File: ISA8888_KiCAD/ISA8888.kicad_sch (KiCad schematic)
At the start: 65 parts, among them J1 Bus_PCI_32bit_Universal, J2 Bus_ISA_16bit, J3 AEN/BALE/TC J3, J4 Crystal J4, J5 PCI Jumpers, J6 PPDGNT# Motherboard Redirect, J7 PPDREQ# Motherboard Redirect, U2 SMROM-AT24CS02, Y1 CFPS-72

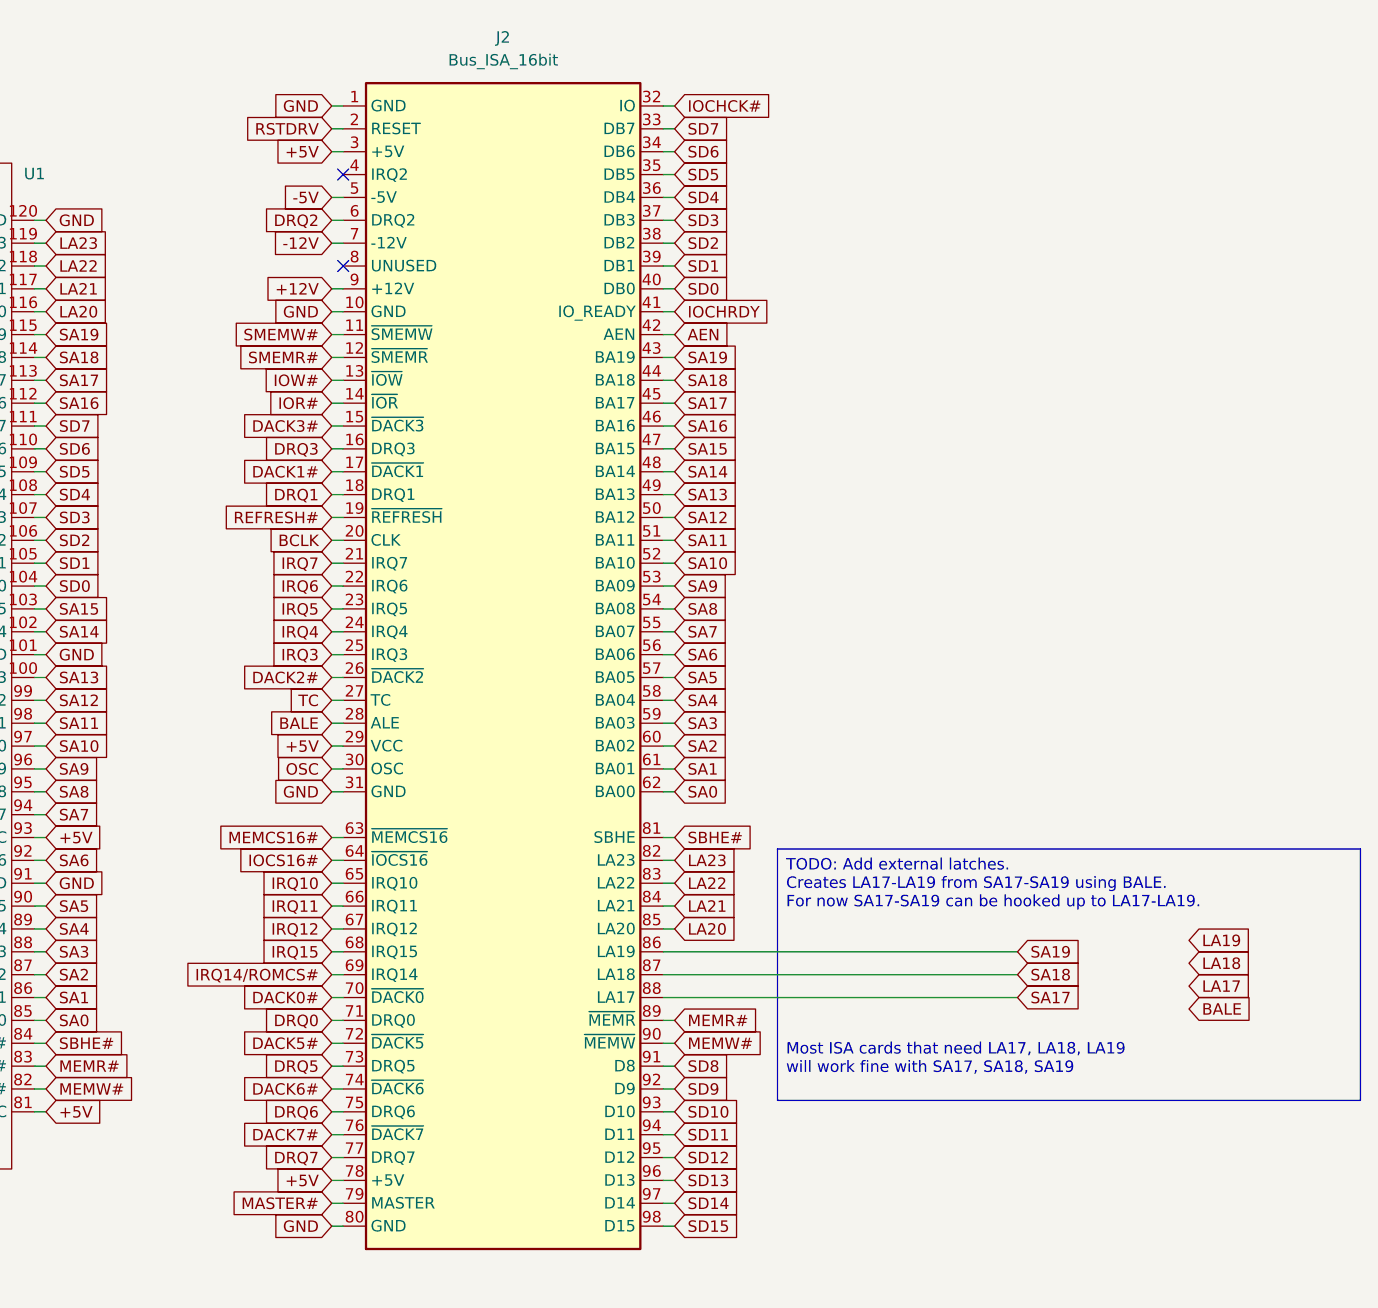
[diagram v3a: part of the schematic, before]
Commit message: IRQ9=IRQ2 Errata
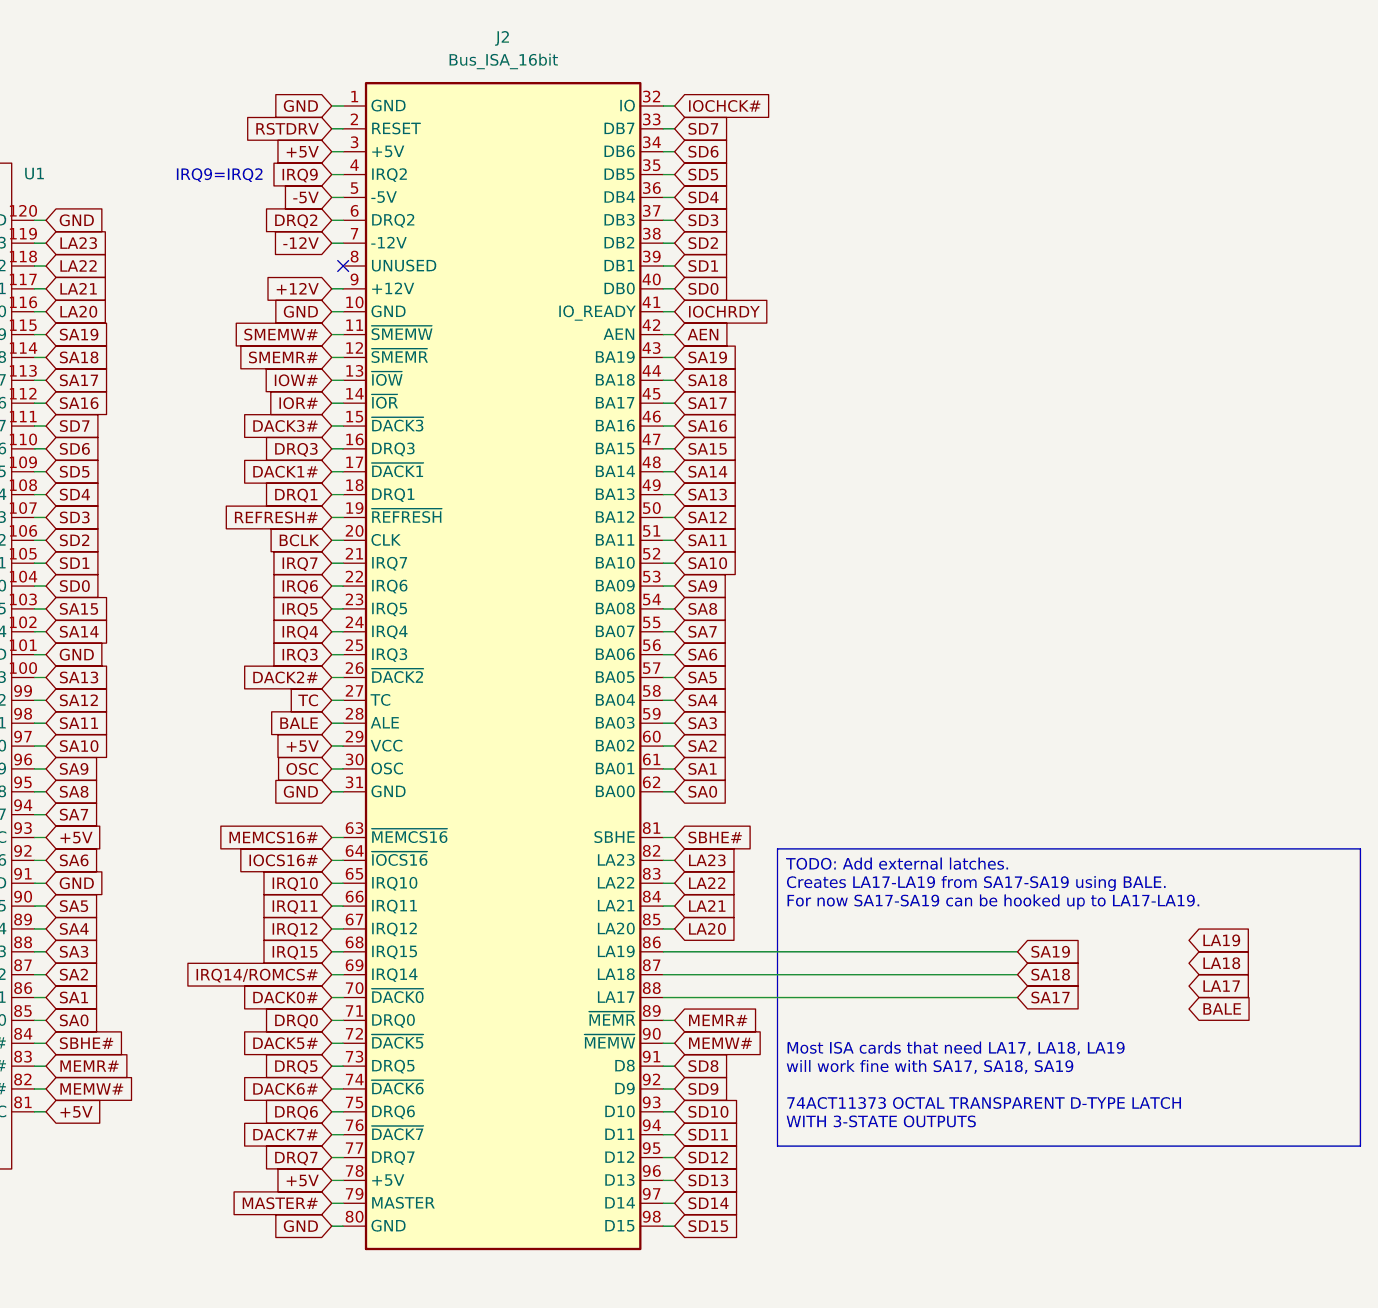
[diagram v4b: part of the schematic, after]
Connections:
- net IRQ9: now also J2.4 (IRQ2)
- no-connect marks 40 -> 39
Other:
- note added: "IRQ9=IRQ2"
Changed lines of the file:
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@@
 		(comment 1 "Inital Pass")
 	)
+	(text "IRQ9=IRQ2\n"
+		(exclude_from_sim no)
+		(at 279.654 38.354 0)
+		(effects
+			(font
+				(size 1.27 1.27)
+			)
+		)
+	)
 	(text "PCI dISAppointment"
 		(exclude_from_sim no)
@@
 		)
 	)
-	(text_box "TODO: Add external latches.\nCreates LA17-LA19 from SA17-SA19 using BALE.\nFor now SA17-SA19 can be hooked up to LA17-LA19.\n\n\n\n\n\n\n\nMost ISA cards that need LA17, LA18, LA19\nwill work fine with SA17, SA18, SA19"
+	(text_box "TODO: Add external latches.\nCreates LA17-LA19 from SA17-SA19 using BALE.\nFor now SA17-SA19 can be hooked up to LA17-LA19.\n\n\n\n\n\n\n\nMost ISA cards that need LA17, LA18, LA19\nwill work fine with SA17, SA18, SA19\n\n74ACT11373 OCTAL TRANSPARENT D-TYPE LATCH\nWITH 3-STATE OUTPUTS "
 		(exclude_from_sim no)
 		(at 341.63 113.03 0)
-		(size 64.77 27.94)
+		(size 64.77 33.02)
 		(margins 0.9525 0.9525 0.9525 0.9525)
 		(stroke
@@
 	)
 	(no_connect
-		(at 293.37 38.1)
-	)
-	(no_connect
 		(at 240.03 201.93)
 	)
@@
 	(wire
 		(pts
+			(xy 292.1 38.1) (xy 293.37 38.1)
+		)
+		(stroke
+			(width 0)
+			(type default)
+		)
+	)
+	(wire
+		(pts
 			(xy 194.31 251.46) (xy 204.47 251.46)
 		)
@@
 			(effects
 				(font
+					(size 1.27 1.27)
+				)
+				(justify right)
+				(hide yes)
+			)
+		)
+	)
+	(global_label "IRQ9"
+		(shape input)
+		(at 292.1 38.1 180)
+		(fields_autoplaced yes)
+		(effects
+			(font
+				(size 1.27 1.27)
+			)
+			(justify right)
+		)
+		(property "Intersheetrefs" "${INTERSHEET_REFS}"
+			(at 284.7 38.1 0)
+			(effects
+				(font

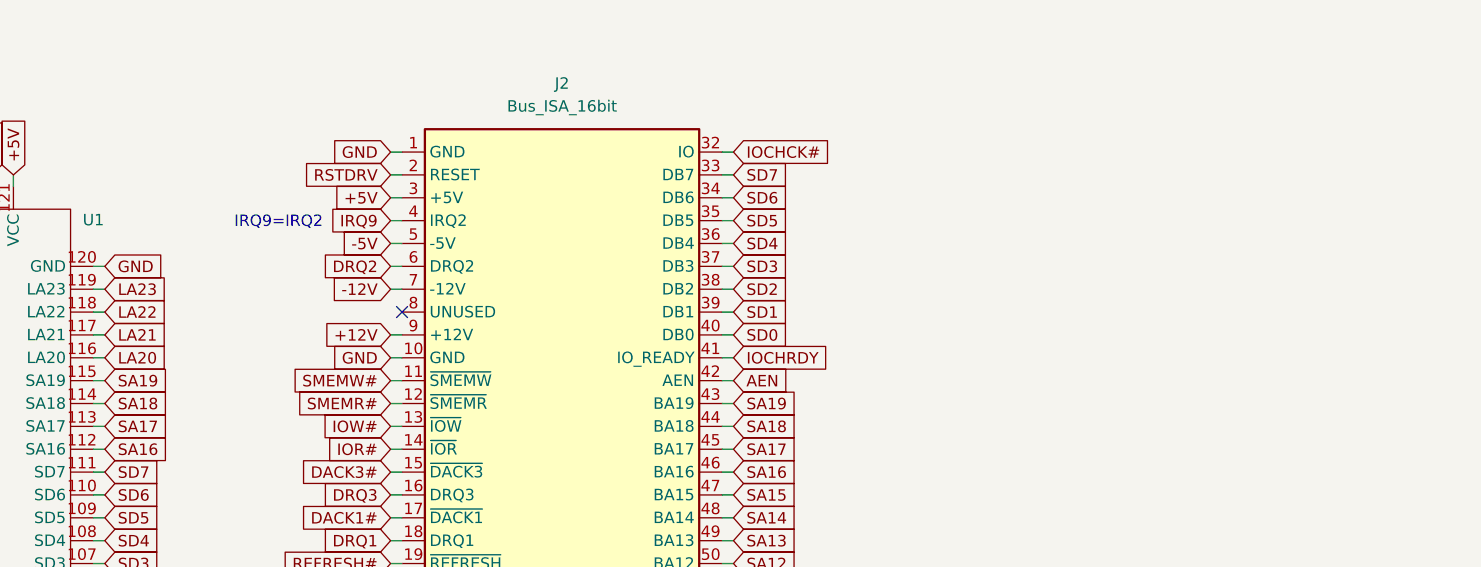
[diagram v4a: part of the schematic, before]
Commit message: Errata 1 NOWS# and IOCHRDY
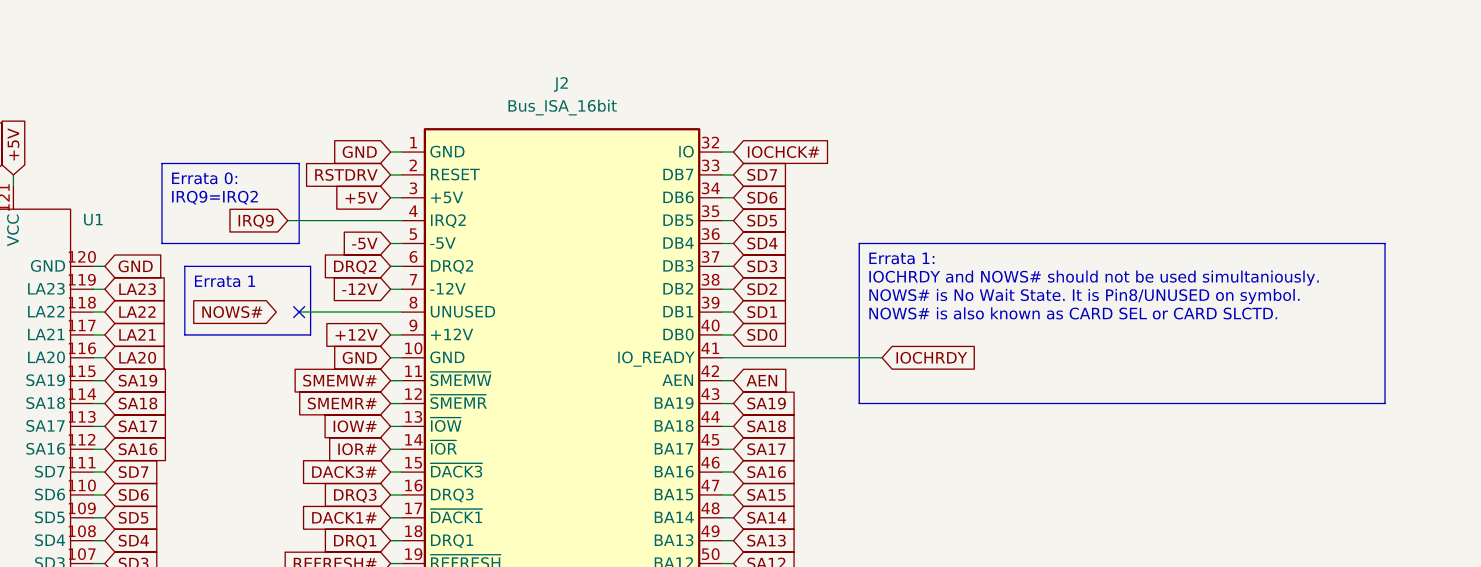
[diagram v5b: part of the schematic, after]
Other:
- note removed: "IRQ9=IRQ2"
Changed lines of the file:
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@@
 		(comment 1 "Inital Pass")
 	)
-	(text "IRQ9=IRQ2\n"
-		(exclude_from_sim no)
-		(at 279.654 38.354 0)
-		(effects
-			(font
-				(size 1.27 1.27)
-			)
-		)
-	)
 	(text "PCI dISAppointment"
 		(exclude_from_sim no)
@@
 		)
 	)
+	(text_box "Errata 1"
+		(exclude_from_sim no)
+		(at 269.24 43.18 0)
+		(size 13.97 7.62)
+		(margins 0.9525 0.9525 0.9525 0.9525)
+		(stroke
+			(width 0)
+			(type solid)
+		)
+		(fill
+			(type none)
+		)
+		(effects
+			(font
+				(size 1.27 1.27)
+			)
+			(justify left top)
+		)
+	)
+	(text_box "Errata 0: \nIRQ9=IRQ2\n"
+		(exclude_from_sim no)
+		(at 266.7 31.75 0)
+		(size 15.24 8.89)
+		(margins 0.9525 0.9525 0.9525 0.9525)
+		(stroke
+			(width 0)
+			(type solid)
+		)
+		(fill
+			(type none)
+		)
+		(effects
+			(font
+				(size 1.27 1.27)
+			)
+			(justify left top)
+		)
+	)
+	(text_box "Errata 1:\nIOCHRDY and NOWS# should not be used simultaniously.\nNOWS# is No Wait State. It is Pin8/UNUSED on symbol.\nNOWS# is also known as CARD SEL or CARD SLCTD."
+		(exclude_from_sim no)
+		(at 344.17 40.64 0)
+		(size 58.42 17.78)
+		(margins 0.9525 0.9525 0.9525 0.9525)
+		(stroke
+			(width 0)
+			(type solid)
+		)
+		(fill
+			(type none)
+		)
+		(effects
+			(font
+				(size 1.27 1.27)
+			)
+			(justify left top)
+		)
+	)
 	(text_box "TODO: Add external latches.\nCreates LA17-LA19 from SA17-SA19 using BALE.\nFor now SA17-SA19 can be hooked up to LA17-LA19.\n\n\n\n\n\n\n\nMost ISA cards that need LA17, LA18, LA19\nwill work fine with SA17, SA18, SA19\n\n74ACT11373 OCTAL TRANSPARENT D-TYPE LATCH\nWITH 3-STATE OUTPUTS "
 		(exclude_from_sim no)
@@
 	)
 	(no_connect
-		(at 293.37 48.26)
+		(at 281.94 48.26)
 	)
 	(no_connect
@@
 	(wire
 		(pts
+			(xy 281.94 48.26) (xy 293.37 48.26)
+		)
+		(stroke
+			(width 0)
+			(type default)
+		)
+	)
+	(wire
+		(pts
 			(xy 292.1 73.66) (xy 293.37 73.66)
 		)
@@
 	(wire
 		(pts
-			(xy 292.1 38.1) (xy 293.37 38.1)
+			(xy 280.67 38.1) (xy 293.37 38.1)
 		)
 		(stroke
@@
 	(wire
 		(pts
-			(xy 330.2 53.34) (xy 328.93 53.34)
+			(xy 346.71 53.34) (xy 328.93 53.34)
 		)
 		(stroke
@@
 	(global_label "IRQ9"
 		(shape input)
-		(at 292.1 38.1 180)
+		(at 280.67 38.1 180)
 		(fields_autoplaced yes)
 		(effects
@@
 		)
 		(property "Intersheetrefs" "${INTERSHEET_REFS}"
-			(at 284.7 38.1 0)
+			(at 273.27 38.1 0)
 			(effects
 				(font
@@
 	(global_label "IOCHRDY"
 		(shape input)
-		(at 330.2 53.34 0)
+		(at 346.71 53.34 0)
 		(fields_autoplaced yes)
 		(effects
@@
 		)
 		(property "Intersheetrefs" "${INTERSHEET_REFS}"
-			(at 341.3496 53.34 0)
+			(at 357.8596 53.34 0)
 			(effects
 				(font
@@
 				(hide yes)
 			)
+		)
+	)
+	(global_label "NOWS#"
+		(shape input)
+		(at 279.4 48.26 180)
+		(fields_autoplaced yes)
+		(effects
+			(font
+				(size 1.27 1.27)
+			)
+			(justify right)
+		)
+		(property "Intersheetrefs" "${INTERSHEET_REFS}"
+			(at 269.8229 48.26 0)
+			(effects
+				(font
+					(size 1.27 1.27)
+				)
+				(justify right)
+				(hide yes)
+			)

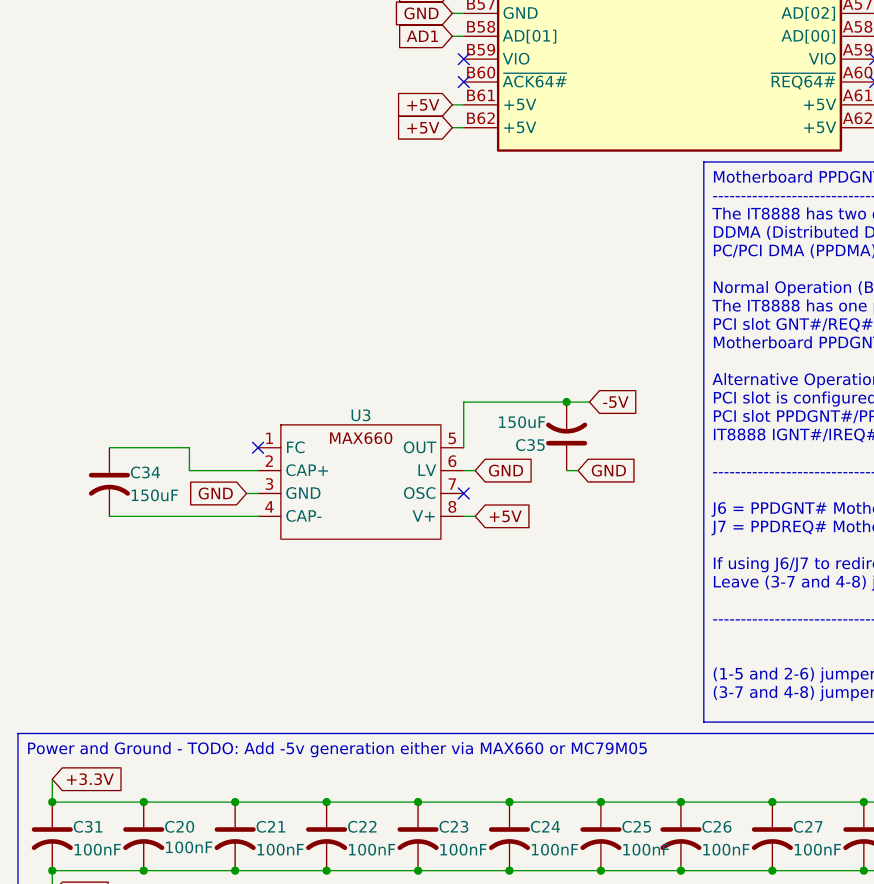
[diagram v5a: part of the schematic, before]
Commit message: Add LM7905 option for -5v instead of MAX660
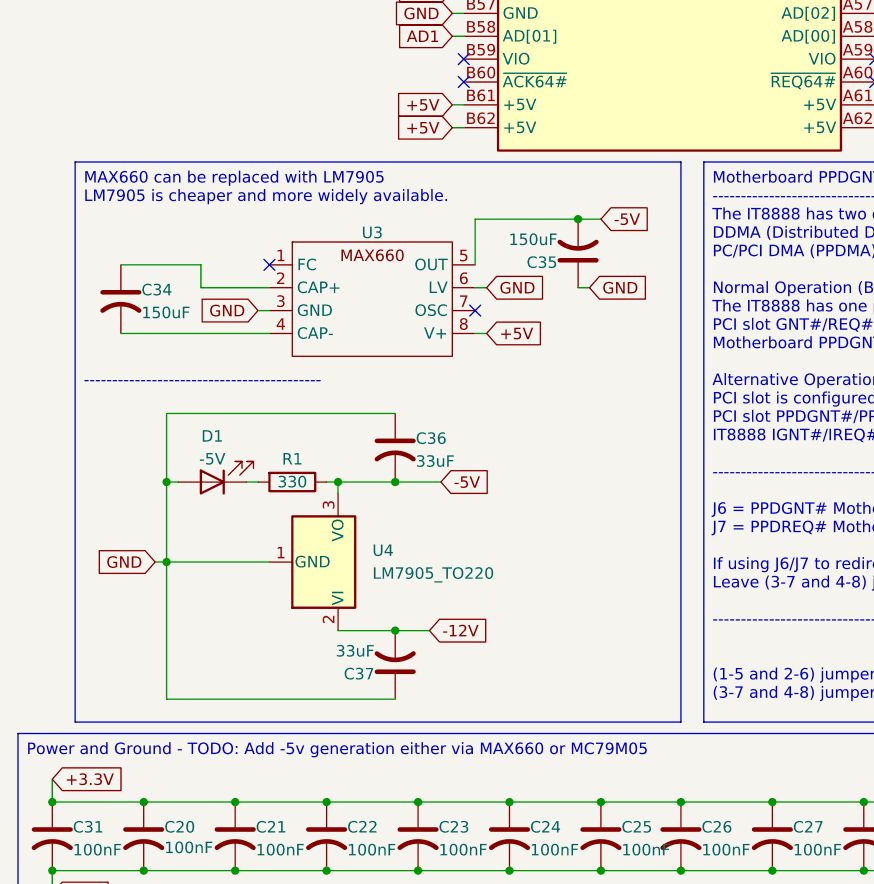
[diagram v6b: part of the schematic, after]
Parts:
- added C36, C37: 33uF, Capacitor_THT:CP_Radial_D5.0mm_P2.50mm, symbol Device:C_US
- added D1: -5V, LED_THT:LED_D5.0mm, symbol Device:LED
- added R1: 330, Resistor_THT:R_Axial_DIN0207_L6.3mm_D2.5mm_P7.62mm_Horizontal, symbol Device:R
- added U4: LM7905_TO220, Package_TO_SOT_THT:TO-220-3_Vertical, symbol Regulator_Linear:LM7905_TO220
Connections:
- net -12V: now also C37.2, U4.2 (VI)
- net -5V: now also C36.2, R1.1, U4.3 (VO)
- net GND: now also C36.1, C37.1, D1.2 (A), U4.1 (GND)
- new net: D1.1 (K), R1.2
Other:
- moved on the sheet: C34, C35, U3

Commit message: New SCH sheet "Power and Configuration"
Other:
- added sheet Power and Configuration (PowerConfig.kicad_sch)
- moved on the sheet: C1, C10, C11, C12, C13, C14, C15, C16, C17, C18, C19, C2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

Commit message: Fixup Power/Config Sheet and update PCB with info from P/C sheet
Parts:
- removed C1, C30, C33: 100uF, Capacitor_THT:CP_Radial_D5.0mm_P2.50mm, symbol Device:C_US
- removed C10, C11, C12, C13, C14, C16, C17, C19, C2, C20, C21, C22, C23, C24, C25, C26, C27, C28, C29, C3, C31, C32, C4, C5, C6, C7, C8, C9: 100nF, Capacitor_SMD:C_1808_4520Metric_Pad1.72x2.30mm_HandSolder, symbol Device:C_US
- removed C15, C18: 47uF, Capacitor_THT:CP_Radial_D5.0mm_P2.50mm, symbol Device:C_US
- removed C34, C35: 150uF, Capacitor_THT:CP_Radial_D5.0mm_P2.50mm, symbol Device:C_US
- removed C36, C37: 33uF, Capacitor_THT:CP_Radial_D5.0mm_P2.50mm, symbol Device:C_US
- removed D1: -5V, LED_THT:LED_D5.0mm, symbol Device:LED
- removed J3: AEN/BALE/TC J3, Connector_PinHeader_2.00mm:PinHeader_2x03_P2.00mm_Vertical, symbol Connector_Generic:Conn_02x03_Odd_Even
- removed J4: Crystal J4, Connector_PinHeader_2.00mm:PinHeader_2x02_P2.00mm_Vertical, symbol Connector_Generic:Conn_02x02_Top_Bottom
- removed J5: PCI Jumpers, Connector_PinHeader_2.00mm:PinHeader_2x04_P2.00mm_Vertical, symbol Connector_Generic:Conn_02x04_Top_Bottom
- removed J6: PPDGNT# Motherboard Redirect, Connector_PinHeader_2.00mm:PinHeader_1x01_P2.00mm_Vertical, symbol Connector:Conn_01x01_Pin
- removed J7: PPDREQ# Motherboard Redirect, Connector_PinHeader_2.00mm:PinHeader_1x01_P2.00mm_Vertical, symbol Connector:Conn_01x01_Pin
- removed R1: 330, Resistor_THT:R_Axial_DIN0207_L6.3mm_D2.5mm_P7.62mm_Horizontal, symbol Device:R
- removed R10, R11, R12, R9: R330, Resistor_THT:R_Axial_DIN0204_L3.6mm_D1.6mm_P5.08mm_Horizontal, symbol Device:R
- removed R13, R14, R3, R4, R5, R6: R4.7K, Resistor_THT:R_Axial_DIN0204_L3.6mm_D1.6mm_P5.08mm_Horizontal, symbol Device:R
- removed R15, R16, R17: R50K, Resistor_THT:R_Axial_DIN0204_L3.6mm_D1.6mm_P5.08mm_Horizontal, symbol Device:R
- removed R7, R8: R1K, Resistor_THT:R_Axial_DIN0204_L3.6mm_D1.6mm_P5.08mm_Horizontal, symbol Device:R
- removed RN1, RN3, RN4: R_Net_10_10k, Resistor_THT:R_Array_SIP11, symbol Device:R_Network10
- removed RN2: R_Net_10_4k7, Resistor_THT:R_Array_SIP11, symbol Device:R_Network10
- removed U2: SMROM-AT24CS02, Package_SO:SOIC-8_3.9x4.9mm_P1.27mm, symbol Memory_EEPROM:AT24CS02-SSHM
- removed U3: ~, Package_SO:SOIC-8_3.9x4.9mm_P1.27mm, symbol ISA8888:MAX660CSAT
- removed U4: LM7905_TO220, Package_TO_SOT_THT:TO-220-3_Vertical, symbol Regulator_Linear:LM7905_TO220
- removed Y1: CFPS-72, Oscillator:Oscillator_SMD_IQD_IQXO70-4Pin_7.5x5.0mm, symbol Oscillator:CFPS-72
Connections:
- no-connect marks 39 -> 26
